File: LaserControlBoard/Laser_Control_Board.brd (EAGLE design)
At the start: 50.8 x 50.8 mm, 37 parts, among them IC1 ULN2803, J1 Servo, J2 FTDI, J5 FEMALE 2x3, U1 ATMEGA328P, Y1 16MHz

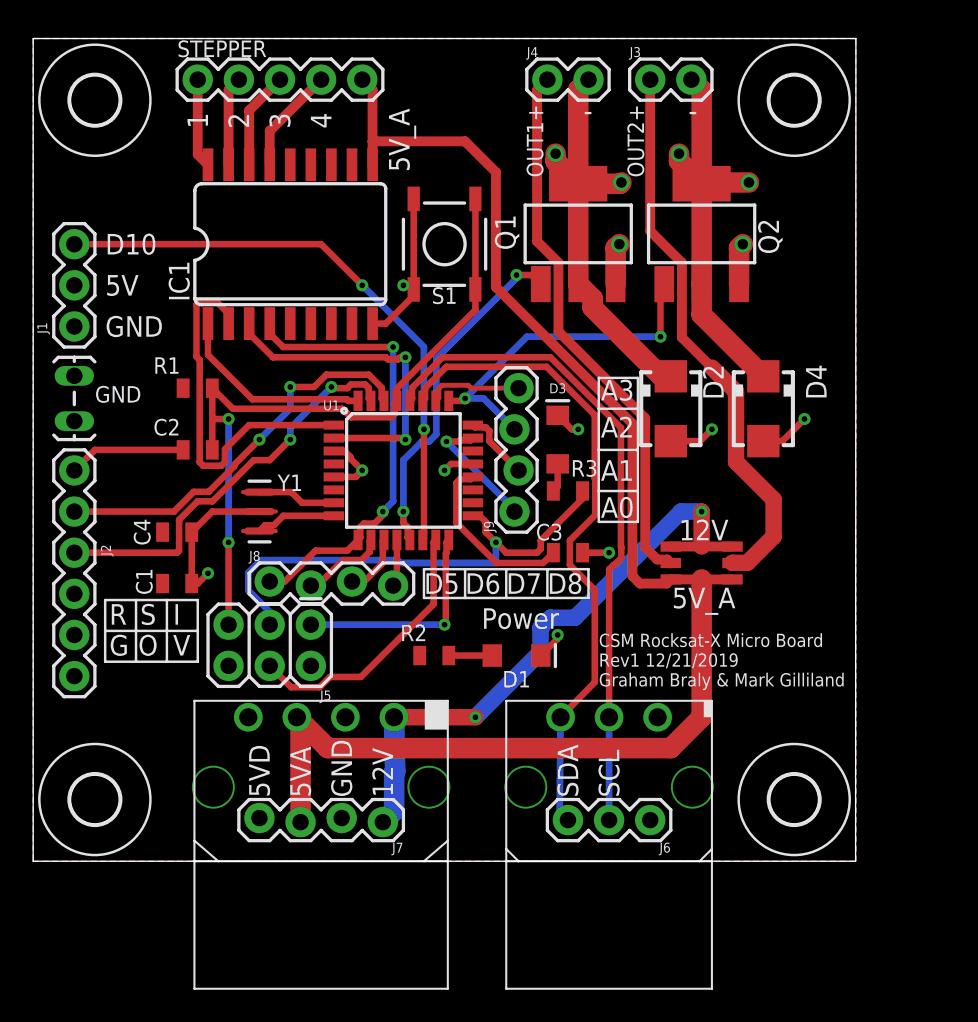
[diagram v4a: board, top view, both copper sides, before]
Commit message: Initial Rev2 for Boom and Exp. Control boards
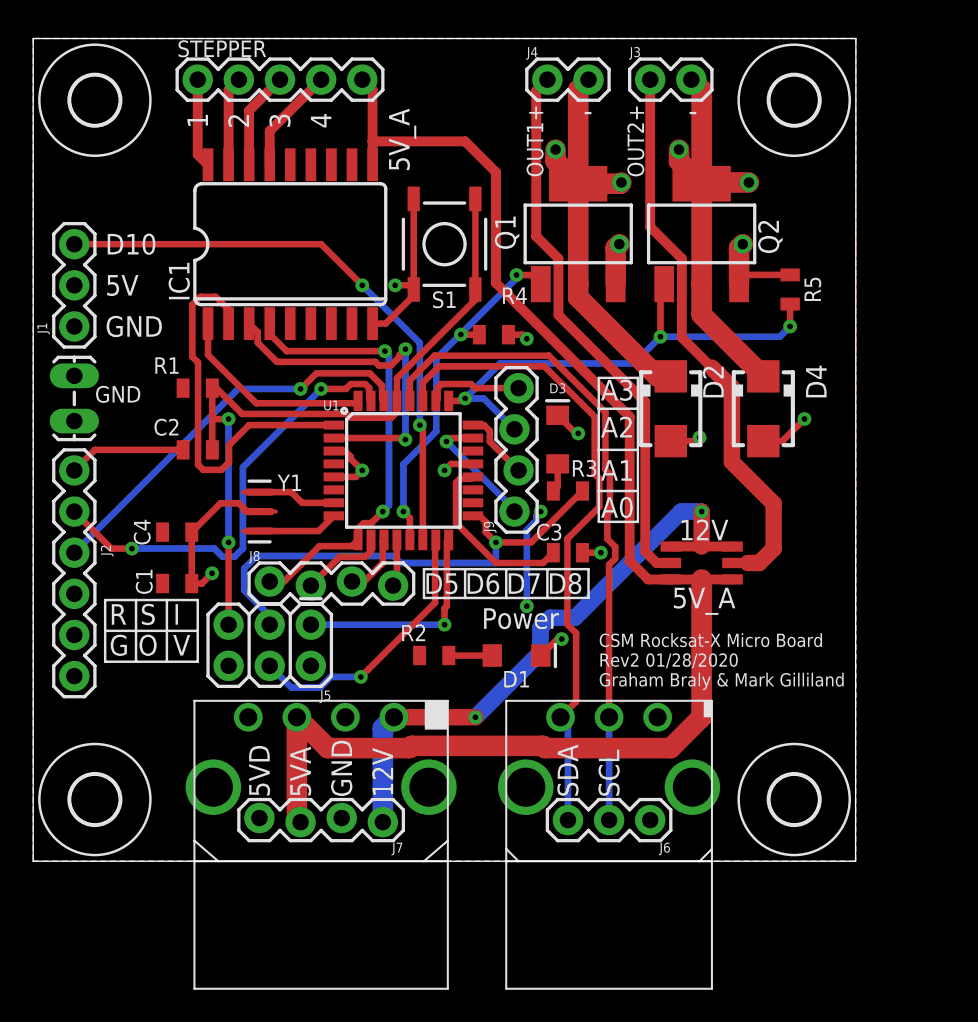
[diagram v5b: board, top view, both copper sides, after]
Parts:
- added R4, R5: 10kΩ, SparkFun-Resistors:0805
- R2, R3: value 1kΩ -> 2.2kΩ
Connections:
- removed net N$6: J2.CTS
- net GND: now also J2.CTS, R4.1, R5.1
- net PB1: now also R4.2
- net PC2: now also R5.2
- net RXI: now also J2.TXO; no longer J2.RXI
- net TXO: now also J2.RXI; no longer J2.TXO
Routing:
- net PC2: track 21.9 -> 31.5 mm, vias 2 -> 3
- net VCC: track 0.00 -> 6.20 mm, vias 0 -> 2
- net GND: track 41.3 -> 45.8 mm, vias 11 -> 12
- net TXO: track 25.1 -> 27.7 mm
- net PD3: track 22.8 -> 24.0 mm
- net PD4: track 20.5 -> 21.6 mm
- net PB1: track 21.4 -> 22.3 mm, vias 2 -> 3
- net PD5: track 28.3 -> 27.5 mm
- net 5V_ACT: track 90.5 -> 89.9 mm
- net RXI: track 24.5 -> 24.9 mm, vias 2 -> 1
- net MOSI: vias 0 -> 1
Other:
- board text added: "CSM Rocksat-X Micro Board Rev2 01/28/2020 Graham Braly & Mark Gilliland"
- board text removed: "CSM Rocksat-X Micro Board Rev1 12/21/2019 Graham Braly & Mark Gilliland"

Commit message: edits to exp and boom control boards
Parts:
- added JP3: (no value), SparkFun-Jumpers:SMT-JUMPER_3_0-NO_TRACE_NO-SILK
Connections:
- new net N$6: IC1.10, JP3.2, STEPPER.5
- net 12V: now also JP3.3
- net 5V_ACT: now also JP3.1; no longer IC1.10, STEPPER.5
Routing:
- net N$6: track 0.00 -> 49.3 mm
- net 5V_ACT: track 89.9 -> 47.5 mm
- net 12V: track 37.9 -> 44.0 mm, vias 2 -> 3
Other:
- board text added: "Stepper Volt."
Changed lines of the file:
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@@
 <text x="4.445" y="32.385" size="1.27" layer="21">GND</text>
 <text x="4.445" y="37.465" size="1.27" layer="21">D10</text>
-<text x="34.925" y="10.795" size="0.8128" layer="21">CSM Rocksat-X Micro Board
+<text x="49.911" y="9.271" size="0.8128" layer="21" rot="R90">CSM Rocksat-X Micro Board
 Rev2 01/28/2020
 Graham Braly &amp; Mark Gilliland</text>
@@
 <wire x1="6.35" y1="16.129" x2="6.35" y2="12.319" width="0.1524" layer="21"/>
 <wire x1="8.255" y1="16.129" x2="8.255" y2="12.319" width="0.1524" layer="21"/>
-<text x="41.402" y="20.447" size="1.27" layer="21" align="center">12V</text>
-<text x="41.402" y="16.256" size="1.27" layer="21" align="center">5V_A</text>
+<text x="42.418" y="13.4874" size="1.27" layer="21" align="center">12V</text>
+<text x="42.926" y="11.2268" size="1.27" layer="21" align="center">5V_A</text>
 <text x="24.13" y="16.51" size="1.27" layer="21">D5</text>
 <text x="26.67" y="16.51" size="1.27" layer="21">D6</text>
@@
 <wire x1="21.844" y1="47.244" x2="22.352" y2="47.244" width="0.1524" layer="51"/>
 <text x="20.32" y="45.466" size="0.8128" layer="51" ratio="12" rot="R90" align="center">COM</text>
+<text x="38.354" y="10.414" size="0.8128" layer="21" rot="R90">Stepper
+Volt.</text>
+<wire x1="45.6184" y1="14.986" x2="45.6184" y2="9.8552" width="0.1524" layer="21"/>
+<wire x1="45.6184" y1="9.8552" x2="41.91" y2="9.8552" width="0.1524" layer="21"/>
+<wire x1="40.894" y1="12.2936" x2="44.704" y2="12.2936" width="0.1524" layer="21"/>
+<wire x1="37.084" y1="14.8844" x2="36.068" y2="14.8844" width="0.1524" layer="21"/>
+<wire x1="36.068" y1="14.8844" x2="36.068" y2="9.906" width="0.1524" layer="21"/>
 </plain>
 <attributes>
@@
 <attribute name="VALUE" x="50.165" y="35.306" size="1.016" layer="27" font="vector" ratio="20" rot="R270" align="top-center"/>
 </element>
+<element name="JP3" library="SparkFun-Jumpers" package="SMT-JUMPER_3_0-NO_TRACE_NO-SILK" value="" x="39.37" y="11.938" smashed="yes" rot="R90">
+<attribute name="VALUE" x="40.513" y="11.938" size="0.6096" layer="27" font="vector" ratio="20" rot="R90" align="top-center"/>
+</element>
 </elements>
 <signals>
@@
 <wire x1="31.321" y1="14.410725" x2="31.944275" y2="15.034" width="1.016" layer="16"/>
 <wire x1="27.305" y1="8.89" x2="31.321" y2="12.906" width="1.016" layer="16"/>
-<wire x1="33.449" y1="15.034" x2="40.005" y2="21.59" width="1.016" layer="16"/>
+<wire x1="33.449" y1="15.034" x2="36.1315" y2="17.7165" width="1.016" layer="16"/>
+<wire x1="36.1315" y1="17.7165" x2="40.005" y2="21.59" width="1.016" layer="16"/>
 <wire x1="31.321" y1="12.906" x2="31.321" y2="14.410725" width="1.016" layer="16"/>
 <wire x1="31.944275" y1="15.034" x2="33.449" y2="15.034" width="1.016" layer="16"/>
@@
 <wire x1="21.59" y1="2.413" x2="21.59" y2="8.2042" width="1.27" layer="16"/>
 <wire x1="21.59" y1="8.2042" x2="22.2758" y2="8.89" width="1.27" layer="16"/>
+<contactref element="JP3" pad="3"/>
+<wire x1="36.1315" y1="17.7165" x2="39.37" y2="14.478" width="0.8128" layer="16"/>
+<wire x1="39.37" y1="14.478" x2="39.37" y2="13.97" width="0.8128" layer="16"/>
+<via x="39.37" y="13.97" extent="1-16" drill="0.35"/>
+<wire x1="39.37" y1="12.954" x2="39.37" y2="13.97" width="0.6096" layer="1"/>
 </signal>
 <signal name="5V_ACT">
 <contactref element="U$1" pad="PIN3"/>
-<contactref element="IC1" pad="10"/>
-<contactref element="STEPPER" pad="5"/>
-<wire x1="20.955" y1="43.0022" x2="20.955" y2="44.45" width="0.6096" layer="1"/>
-<wire x1="20.955" y1="44.45" x2="20.955" y2="47.625" width="0.6096" layer="1"/>
-<wire x1="20.955" y1="47.625" x2="20.32" y2="48.26" width="0.6096" layer="1"/>
 <contactref element="JP1" pad="1"/>
 <contactref element="JP2" pad="1"/>
 <wire x1="39.37" y1="17.399" x2="41.275" y2="17.399" width="0.6096" layer="1"/>
 <wire x1="41.275" y1="17.399" x2="43.18" y2="17.399" width="0.6096" layer="1"/>
-<wire x1="28.575" y1="42.545" x2="28.575" y2="35.70505625" width="0.6096" layer="1"/>
-<wire x1="28.575" y1="42.545" x2="26.67" y2="44.45" width="0.6096" layer="1"/>
-<wire x1="26.67" y1="44.45" x2="20.955" y2="44.45" width="0.6096" layer="1"/>
 <contactref element="J7" pad="3"/>
 <wire x1="39.37" y1="6.985" x2="41.275" y2="8.89" width="1.27" layer="1"/>
-<wire x1="41.275" y1="8.89" x2="41.275" y2="17.399" width="1.27" layer="1"/>
+<wire x1="41.275" y1="8.89" x2="41.275" y2="10.922" width="1.27" layer="1"/>
+<wire x1="41.275" y1="10.922" x2="41.275" y2="17.399" width="1.27" layer="1"/>
 <wire x1="23.23773125" y1="6.985" x2="23.37743125" y2="7.1247" width="1.27" layer="1"/>
 <wire x1="31.47386875" y1="7.1247" x2="31.61356875" y2="6.985" width="1.27" layer="1"/>
 <wire x1="31.61356875" y1="6.985" x2="39.37" y2="6.985" width="1.27" layer="1"/>
 <wire x1="23.37743125" y1="7.1247" x2="31.47386875" y2="7.1247" width="1.27" layer="1"/>
-<wire x1="28.575" y1="35.70505625" x2="36.83" y2="27.45005625" width="0.6096" layer="1"/>
-<wire x1="37.973" y1="17.399" x2="39.37" y2="17.399" width="0.6096" layer="1"/>
-<wire x1="36.83" y1="27.45005625" x2="36.83" y2="18.542" width="0.6096" layer="1"/>
-<wire x1="36.83" y1="18.542" x2="37.973" y2="17.399" width="0.6096" layer="1"/>
 <wire x1="16.2814" y1="8.89" x2="16.2814" y2="2.6416" width="1.27" layer="1"/>
 <wire x1="16.2814" y1="2.6416" x2="16.51" y2="2.413" width="1.27" layer="1"/>
 <wire x1="16.2814" y1="8.89" x2="18.1864" y2="6.985" width="1.27" layer="1"/>
 <wire x1="18.1864" y1="6.985" x2="23.23773125" y2="6.985" width="1.27" layer="1"/>
+<contactref element="JP3" pad="1"/>
+<wire x1="39.37" y1="10.922" x2="41.275" y2="10.922" width="0.6096" layer="1"/>
 </signal>
 <signal name="SDA">
@@
 <wire x1="35.9382" y1="18.68291875" x2="35.56" y2="18.30471875" width="0.4064" layer="1"/>
 <wire x1="35.45356875" y1="21.44243125" x2="35.45356875" y2="19.9017125" width="0.4064" layer="1"/>
-<wire x1="35.56" y1="18.30471875" x2="35.56" y2="8.89" width="0.4064" layer="1"/>
+<wire x1="35.56" y1="18.30471875" x2="35.56" y2="17.018" width="0.4064" layer="1"/>
+<wire x1="35.56" y1="17.018" x2="35.56" y2="8.89" width="0.4064" layer="1"/>
 </signal>
 <signal name="PB2">
@@
 <wire x1="22.46" y1="17.253" x2="22.225" y2="17.018" width="0.4064" layer="1"/>
 </signal>
+<signal name="N$6">
+<contactref element="IC1" pad="10"/>
+<contactref element="JP3" pad="2"/>
+<contactref element="STEPPER" pad="5"/>
+<wire x1="39.37" y1="11.938" x2="37.846" y2="11.938" width="0.8128" layer="1"/>
+<wire x1="37.846" y1="11.938" x2="36.8272" y2="12.9568" width="0.8128" layer="1"/>
+<wire x1="30.988" y1="33.782" x2="30.226" y2="33.782" width="0.8128" layer="1"/>
+<wire x1="30.226" y1="33.782" x2="28.448" y2="35.56" width="0.8128" layer="1"/>
+<wire x1="27.3558" y1="43.0022" x2="20.955" y2="43.0022" width="0.8128" layer="1"/>
+<wire x1="36.8272" y1="12.9568" x2="36.8272" y2="27.9428" width="0.8128" layer="1"/>
+<wire x1="36.8272" y1="27.9428" x2="30.988" y2="33.782" width="0.8128" layer="1"/>
+<wire x1="28.448" y1="35.56" x2="28.448" y2="41.91" width="0.8128" layer="1"/>
+<wire x1="28.448" y1="41.91" x2="27.3558" y2="43.0022" width="0.8128" layer="1"/>
+<wire x1="20.955" y1="43.0022" x2="20.955" y2="47.625" width="0.8128" layer="1"/>
+<wire x1="20.955" y1="47.625" x2="20.32" y2="48.26" width="0.8128" layer="1"/>
+</signal>
 </signals>
